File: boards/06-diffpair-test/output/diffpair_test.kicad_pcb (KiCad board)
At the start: 4 copper layers, 100 x 80 mm, 7 parts, among them J1 USB-C, J3 MiniPCIe, J4 FFC4, U1 QFN32_USB2, U2 BGA49_USB3, U3 QFP48_PCIe, U4 QFN24_MIPI

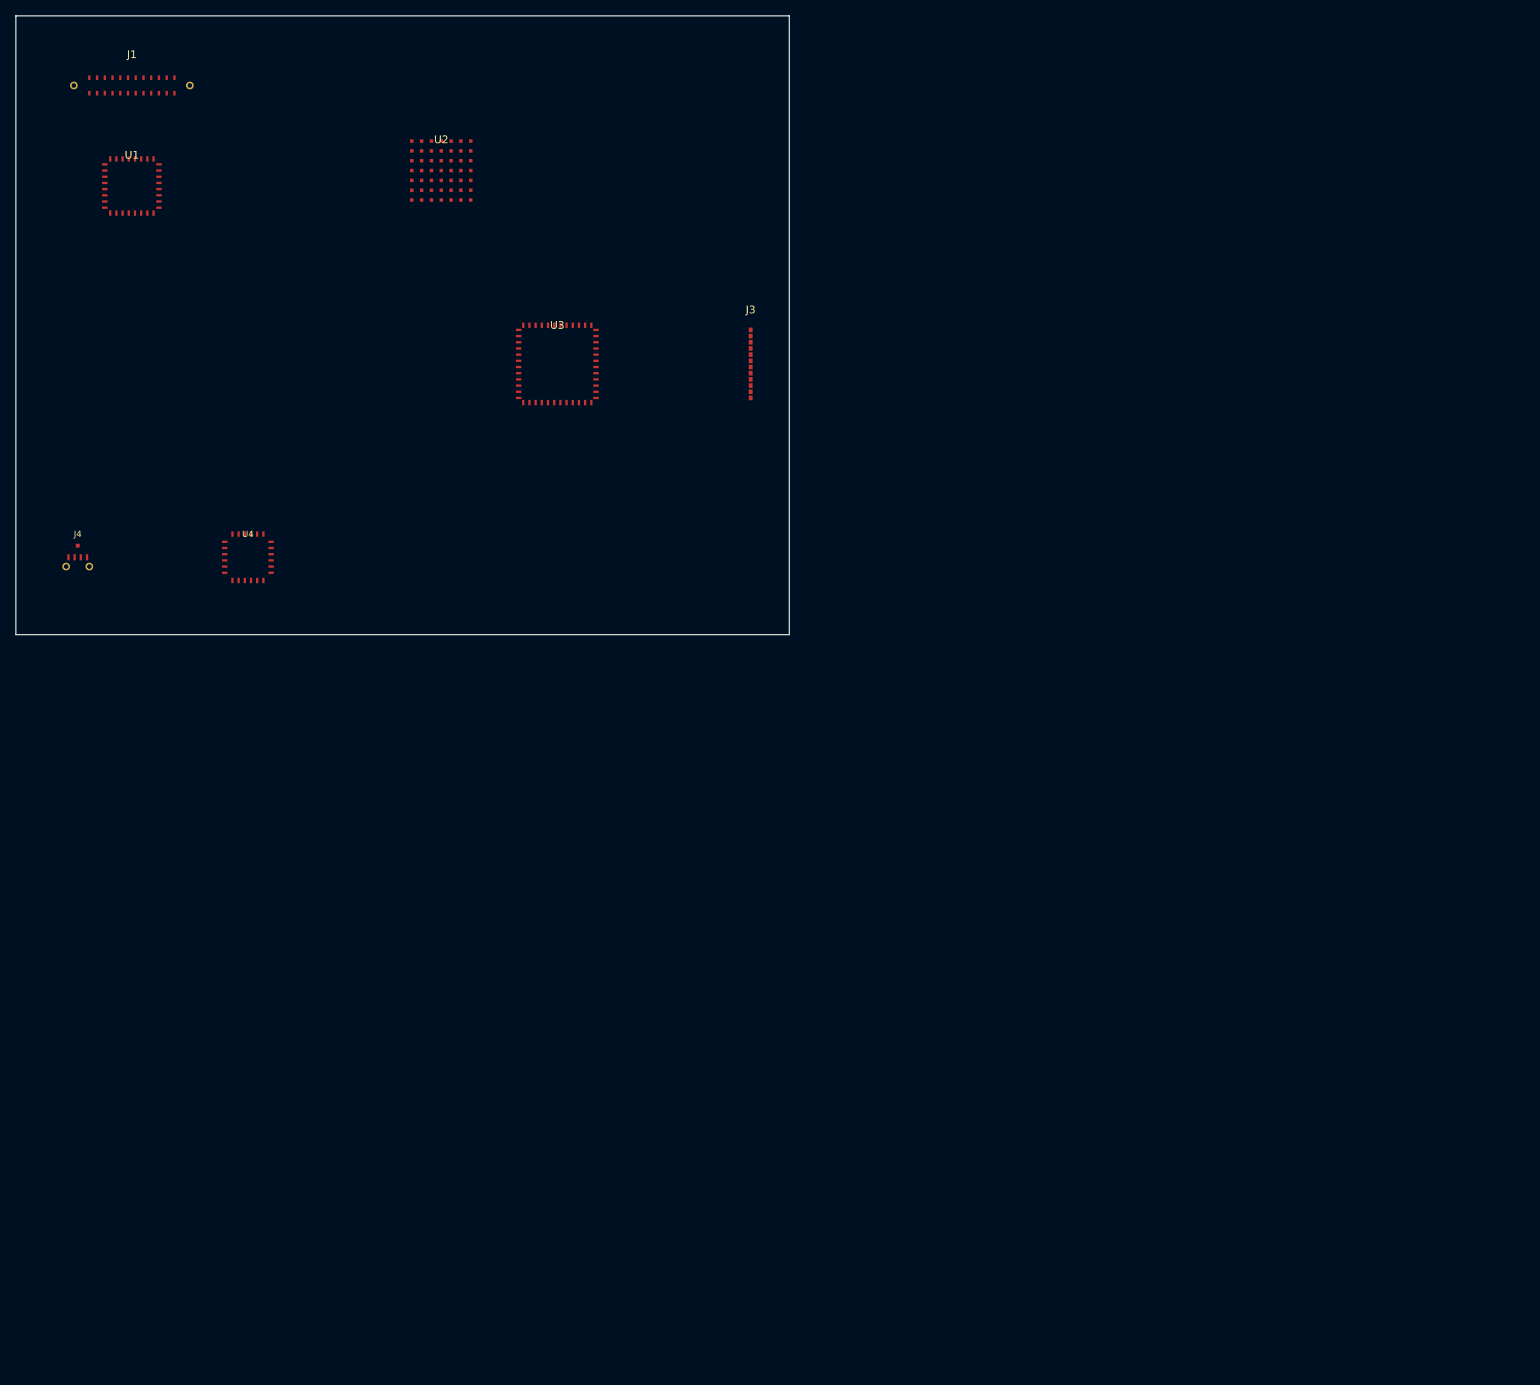
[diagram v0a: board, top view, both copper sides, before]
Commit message: fix(pcb): page-fit routed boards only; revert unrouted sources (refs #3714)
page_fit was applied to and committed for the UNROUTED board sources too.
Because the autorouter is absolute-grid-position-dependent, translating the
unrouted boards changed routing outcomes and turned CI red on three jobs:
- Test: board-02 re-route produced a platform-specific segment count.
- Diff-Pair (06) / Match-Group (07): re-routing the moved unrouted boards
  fractured plane nets under the copper-union pour audit (#3509/#3617).

page_fit is a pure post-route translation, so it must touch the ROUTED
output only:
- Revert every unrouted boards/*/output/<name>.kicad_pcb to origin/main
  (byte-identical); keep the page-fitted *_routed.kicad_pcb (gallery/viewer).
- Revert tests/router/test_board02_manufacturable_baseline.py to main
  (unrouted board-02 unchanged -> reproduces main's result).
- Build hook: _run_step_page_fit now operates on the routed PCB only and
  skips cleanly when no routed output exists, instead of falling back to and
  persisting a page-fit unrouted PCB.

Retains the sound geometry fixes (translation-invariant
point_to_segment_distance, _format_coord_mm, diffpair +1e-6 window tolerance).

Co-Authored-By: Claude Opus 4.7 <noreply@anthropic.com>
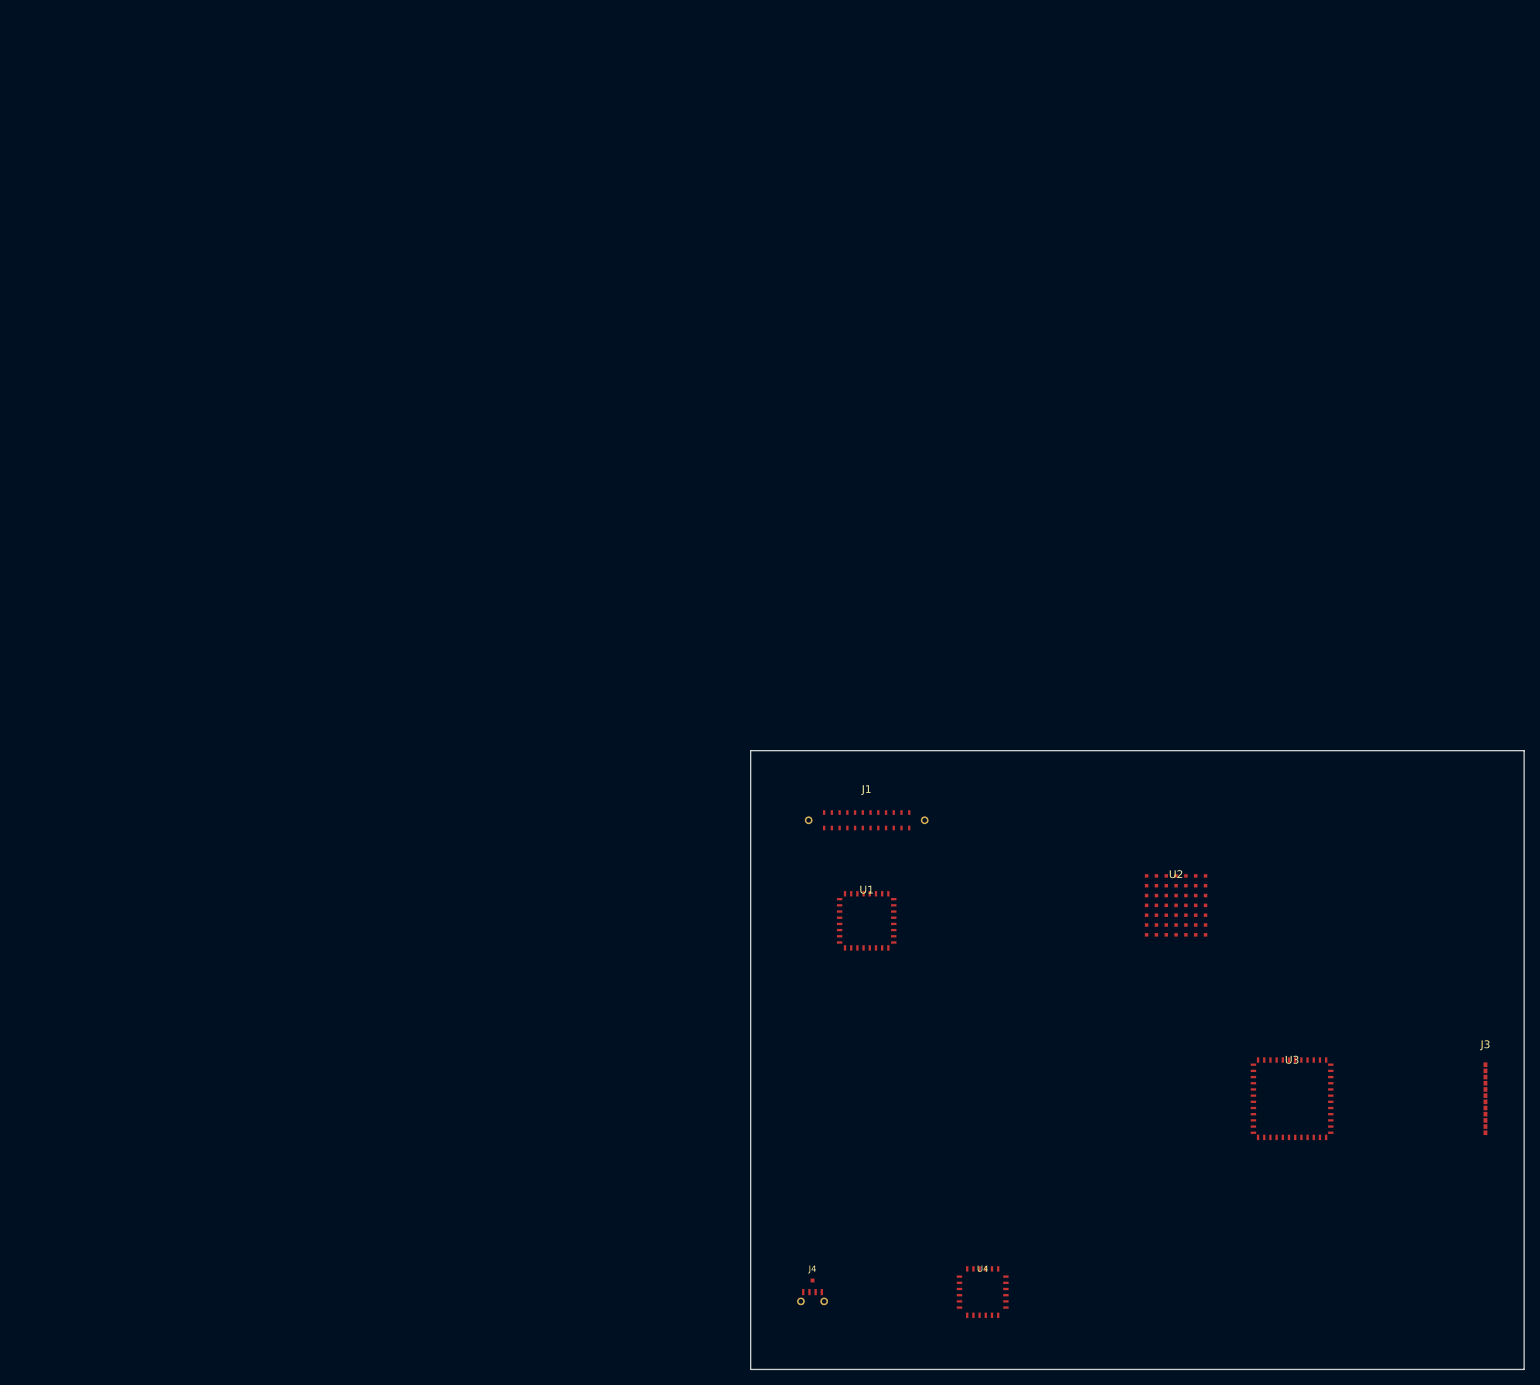
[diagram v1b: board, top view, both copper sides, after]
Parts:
- moved J1 134.4 mm to (115.0, 108.0)
- moved J3 134.4 mm to (195.0, 145.0)
- moved J4 134.4 mm to (108.0, 170.0)
- moved U1 134.4 mm to (115.0, 122.0)
- moved U2 134.4 mm to (155.0, 120.0)
- moved U3 134.4 mm to (170.0, 145.0)
- moved U4 134.4 mm to (130.0, 170.0)

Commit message: feat(pcb): add page_fit to size sheet to board + center, apply to all boards
Add PCB.page_fit(margin=5.0) which rewrites the (paper ...) node to a tight
(paper "User" W H) sized to the Edge.Cuts bbox plus a uniform margin and
translates every board item (footprints, segments, vias, zones incl.
filled_polygons, gr_* graphics, text) so the board is centered with that
margin. Pure geometric translate — relative geometry, routing and DRC
validity are preserved, no re-route needed.

Expose it as `kct pcb page-fit <pcb> [-o out] [--margin] [--dry-run]` and
wire a PAGE_FIT build step (after stitch, before verify/export) so future
boards are centered too. Apply page_fit to all demo boards (00-07 +
external/softstart), both routed and unrouted PCBs, so the committed
layouts fill + center the KiCanvas viewer instead of sitting tiny in an A4
page. Boards 00/01 stay DRC-clean (0 errors); no board's DRC count changed.

Co-Authored-By: Claude Opus 4.7 <noreply@anthropic.com>
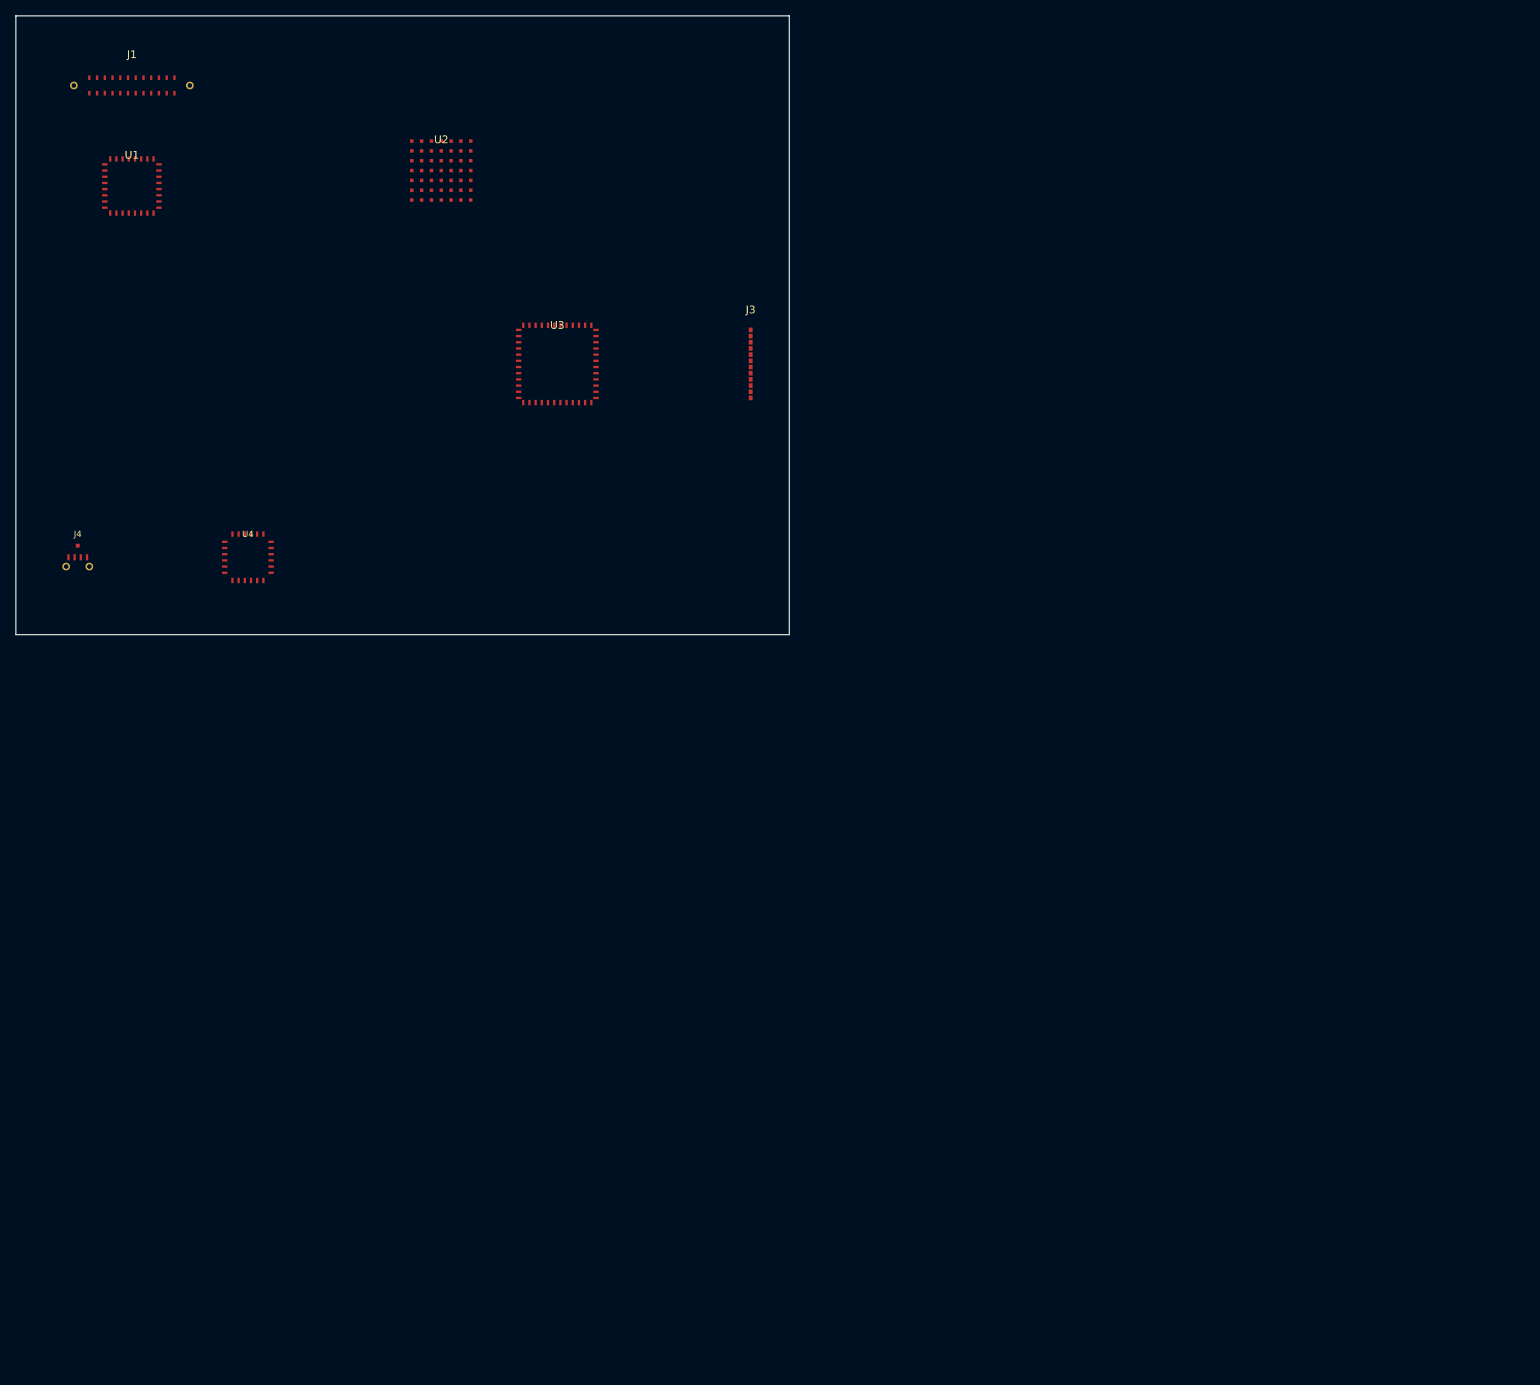
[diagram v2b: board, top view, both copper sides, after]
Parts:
- moved J1 134.4 mm to (20.0, 13.0)
- moved J3 134.4 mm to (100.0, 50.0)
- moved J4 134.4 mm to (13.0, 75.0)
- moved U1 134.4 mm to (20.0, 27.0)
- moved U2 134.4 mm to (60.0, 25.0)
- moved U3 134.4 mm to (75.0, 50.0)
- moved U4 134.4 mm to (35.0, 75.0)
